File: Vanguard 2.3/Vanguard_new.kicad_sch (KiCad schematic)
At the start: 86 parts, among them J1 USB_C_Receptacle_USB2.0_16P, J2 Conn_02x03_Pin, J3 Micro_SD_Card_Det1, J4 STARBOARD_SERVO, J5 PORTSIDE_SERVO, J6 Battery In, J7 EJECTION_SERVO, Q1 BSS138, Q2 BSS138, Q3 BSS138, Q4 BSS138, U1 ATSAMD11D14A-M, U2 ATmega4809-A, U3 AT25DF641A-SH-T, U4 AP2112K-3.3, U5 BD1020HFV, U6 BNO086, U7 TXB0104D, U8 TPS61092, U9 MPM3610AGQV-P, Y1 32.768kHz

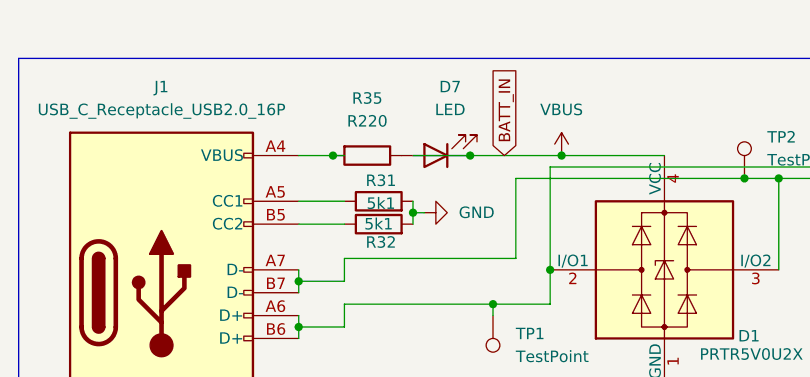
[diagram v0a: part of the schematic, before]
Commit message: Chnaged the led seires to parallel
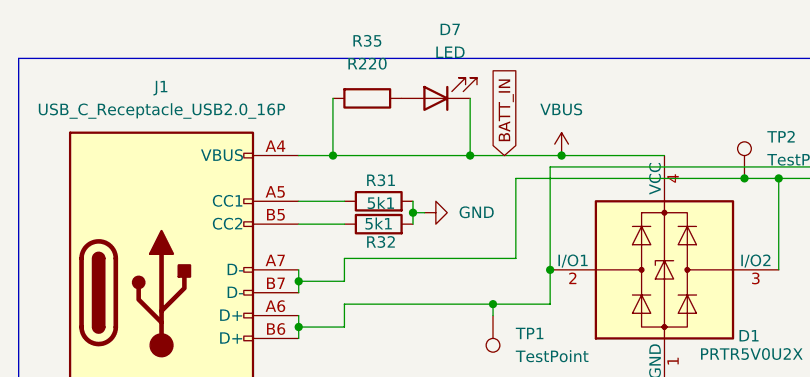
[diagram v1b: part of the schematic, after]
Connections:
- net VBUS: now also J1.A4 (VBUS), J1.A9 (VBUS), J1.B4 (VBUS), J1.B9 (VBUS), R35.2
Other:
- moved on the sheet: D7, R35
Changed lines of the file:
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@@
 	)
 	(junction
-		(at 62.23 24.13)
-		(diameter 0)
-		(color 0 0 0 0)
-	)
-	(junction
 		(at 323.85 54.61)
 		(diameter 0)
@@
 	)
 	(junction
+		(at 62.23 24.13)
+		(diameter 0)
+		(color 0 0 0 0)
+	)
+	(junction
 		(at 393.7 154.94)
 		(diameter 0)
@@
 	(wire
 		(pts
-			(xy 55.88 24.13) (xy 62.23 24.13)
-		)
-		(stroke
-			(width 0)
-			(type default)
-		)
-	)
-	(wire
-		(pts
 			(xy 45.72 54.61) (xy 52.07 54.61)
 		)
@@
 	(wire
 		(pts
-			(xy 46.99 24.13) (xy 48.26 24.13)
+			(xy 62.23 17.78) (xy 62.23 24.13)
+		)
+		(stroke
+			(width 0)
+			(type default)
+		)
+	)
+	(wire
+		(pts
+			(xy 46.99 24.13) (xy 62.23 24.13)
+		)
+		(stroke
+			(width 0)
+			(type default)
+		)
+	)
+	(wire
+		(pts
+			(xy 46.99 17.78) (xy 46.99 24.13)
 		)
 		(stroke
@@
 	(label "RX_UPDI"
 		(at 153.67 50.8 0)
-		(fields_autoplaced yes)
 		(effects
 			(font
@@
 	(label "TX_UPDI"
 		(at 153.67 48.26 0)
-		(fields_autoplaced yes)
 		(effects
 			(font
@@
 	(symbol
 		(lib_id "Device:LED")
-		(at 58.42 24.13 180)
+		(at 58.42 17.78 180)
 		(unit 1)
 		(exclude_from_sim no)
@@
 		(fields_autoplaced yes)
 		(property "Reference" "D7"
-			(at 60.0075 16.51 0)
+			(at 60.0075 10.16 0)
 			(effects
 				(font
@@
 		)
 		(property "Value" "LED"
-			(at 60.0075 19.05 0)
+			(at 60.0075 12.7 0)
 			(effects
 				(font
@@
 		)
 		(property "Footprint" "LED_SMD:LED_0201_0603Metric"
-			(at 58.42 24.13 0)
+			(at 58.42 17.78 0)
 			(effects
 				(font
@@
 		)
 		(property "Datasheet" "~"
-			(at 58.42 24.13 0)
+			(at 58.42 17.78 0)
 			(effects
 				(font
@@
 		)
 		(property "Description" "Light emitting diode"
-			(at 58.42 24.13 0)
+			(at 58.42 17.78 0)
 			(effects
 				(font
@@
 	(symbol
 		(lib_id "Device:R")
-		(at 50.8 24.13 270)
+		(at 50.8 17.78 270)
 		(unit 1)
 		(exclude_from_sim no)
@@
 		(fields_autoplaced yes)
 		(property "Reference" "R35"
-			(at 50.8 17.78 90)
+			(at 50.8 11.43 90)
 			(effects
 				(font
@@
 		)
 		(property "Value" "R220"
-			(at 50.8 20.32 90)
+			(at 50.8 13.97 90)
 			(effects
 				(font
@@
 		)
 		(property "Footprint" "Resistor_SMD:R_0402_1005Metric"
-			(at 50.8 22.352 90)
+			(at 50.8 16.002 90)
 			(effects
 				(font
@@
 		)
 		(property "Datasheet" "~"
-			(at 50.8 24.13 0)
+			(at 50.8 17.78 0)
 			(effects
 				(font
@@
 		)
 		(property "Description" "Resistor"
-			(at 50.8 24.13 0)
+			(at 50.8 17.78 0)
 			(effects
 				(font

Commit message: removed usbc shield hybrid ground + small changes
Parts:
- removed BZ1: Buzzer, Buzzer_Beeper:Buzzer_TDK_PS1240P02BT_D12.2mm_H6.5mm, symbol Device:Buzzer
- removed C1: 4n7, Capacitor_SMD:C_0201_0603Metric, symbol Device:C
- removed R1: 1M, Resistor_SMD:R_0402_1005Metric, symbol Device:R
